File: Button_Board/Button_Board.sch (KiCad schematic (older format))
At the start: 8 parts, among them J1 Conn_01x10, SW1 SW_Push, SW2 SW_Push, SW3 SW_Push, SW4 SW_Push, SW5 SW_Push, SW6 SW_Push, SW7 SW_Push

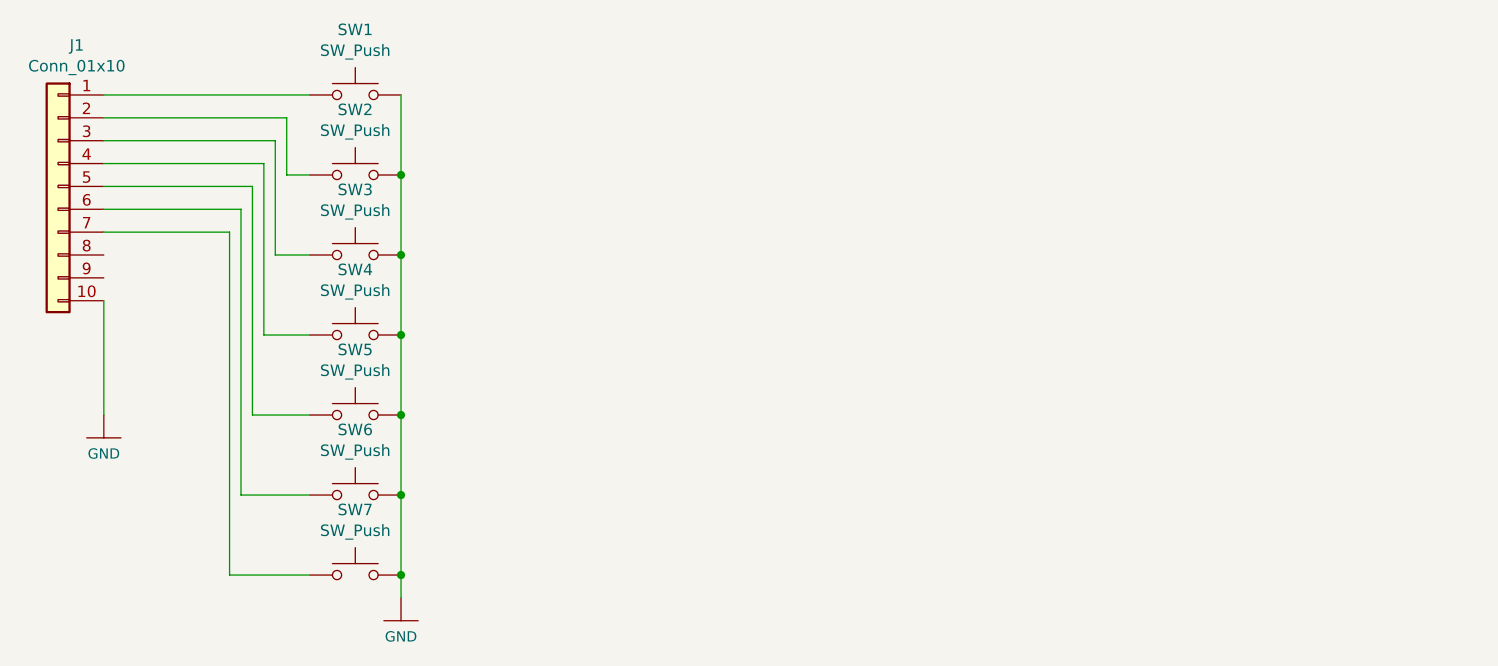
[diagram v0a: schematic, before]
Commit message: Button board layout with mini joystick
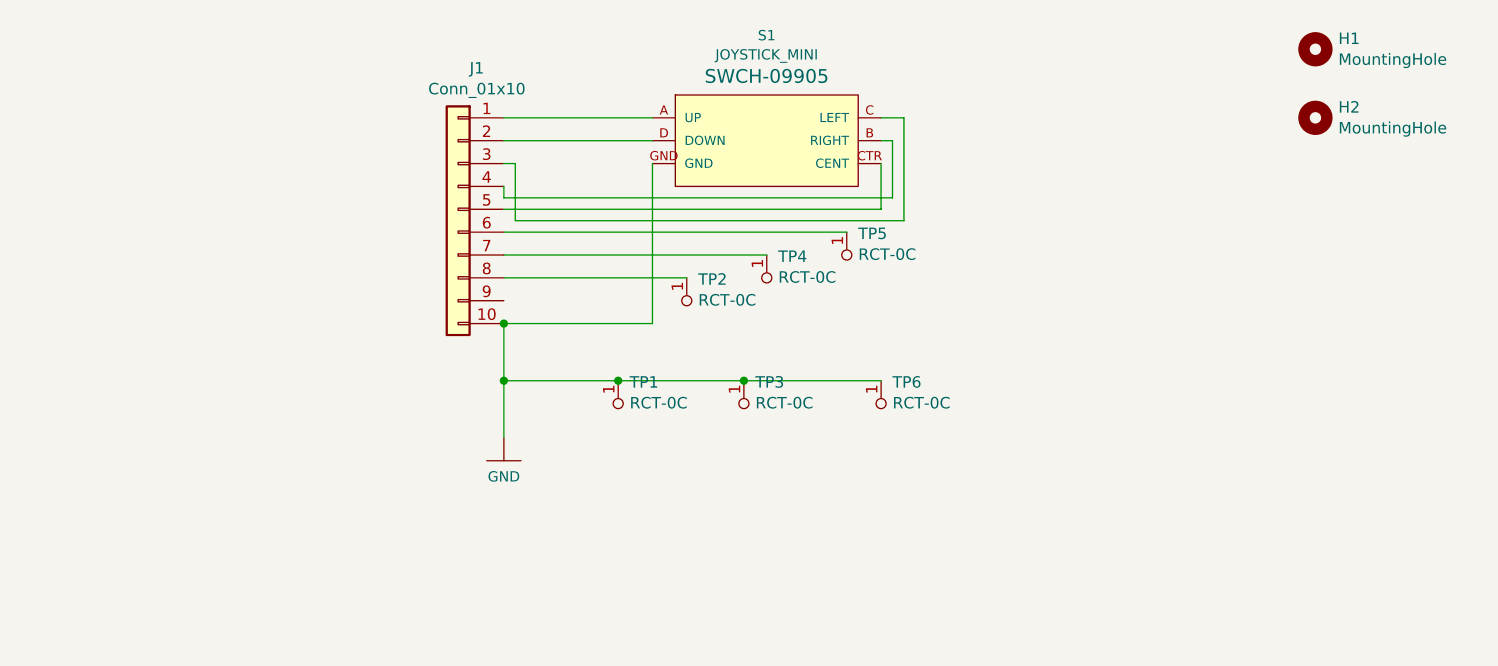
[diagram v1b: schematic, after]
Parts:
- removed SW1, SW2, SW3, SW4, SW5, SW6, SW7: SW_Push, Button_Switch_SMD:SW_SPST_TL3342, symbol Switch:SW_Push
- added H1, H2: MountingHole, MountingHole:MountingHole_2.2mm_M2_ISO7380_Pad, symbol Mechanical:MountingHole
- added S1: JOYSTICK_MINI, JOYSTICK_MINI, symbol SparkFun-Switches:JOYSTICK_MINI
- added TP1, TP2, TP3, TP4, TP5, TP6: RCT-0C, digikey-footprints:PROBE_PAD_0805, symbol dk_Test-Points:RCT-0C
- J1: footprint Connector_JST:JST_PH_S10B-PH-SM4-TB_1x10-1MP_P2.00mm_Horizontal -> Connector_JST:JST_PH_B10B-PH-SM4-TB_1x10-1MP_P2.00mm_Vertical
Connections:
- net GND: now also S1.GND, TP1.1, TP3.1, TP6.1
- net at J1.1 (Pin_1): now also S1.A (UP)
- net at J1.2 (Pin_2): now also S1.D (DOWN)
- net at J1.3 (Pin_3): now also S1.C (LEFT)
- net at J1.4 (Pin_4): now also S1.B (RIGHT)
- net at J1.5 (Pin_5): now also S1.CTR (CENT)
- net at J1.6 (Pin_6): now also TP5.1
- net at J1.7 (Pin_7): now also TP4.1
- net at J1.8 (Pin_8): now also TP2.1
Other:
- moved on the sheet: J1
